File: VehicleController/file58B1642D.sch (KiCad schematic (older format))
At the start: 41 parts, among them J10 CONN_01X12, J8 CONN_01X03, J9 CONN_01X12, Q5 Q_PMOS_GSD, Q6 MC_FET, Q7 PC_FET, U16 MC_Override, U17 MCR_Shtdwn, U18 MCL_Shtdwn, U19 RI-0505S, U20 ISO1540, U21 TCMT1103, U22 TLP293-4, U23 PC_RLY, U24 MCP47FEBX2

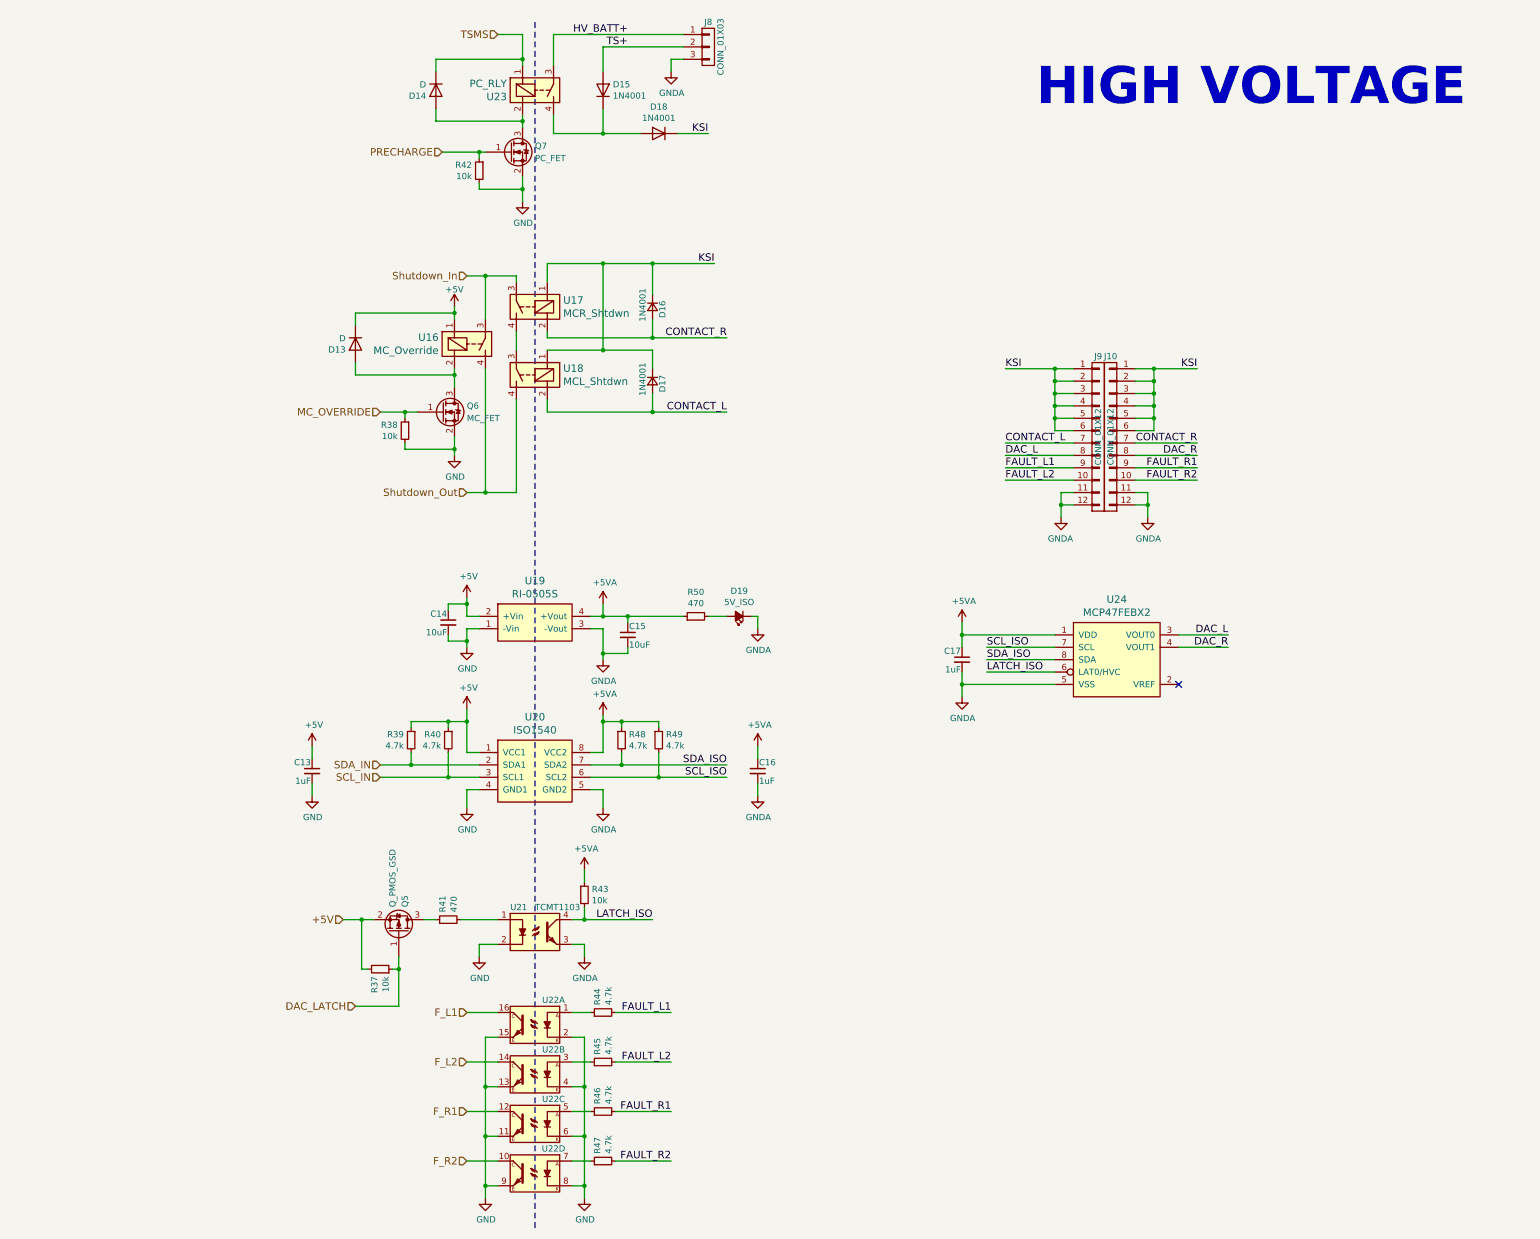
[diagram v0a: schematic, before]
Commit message: Revert "MX120, GDS->GSD FETs on VCU"
This reverts commit 5f93bf7ab8a0e63cb004bd031bee3d8b2541593f.
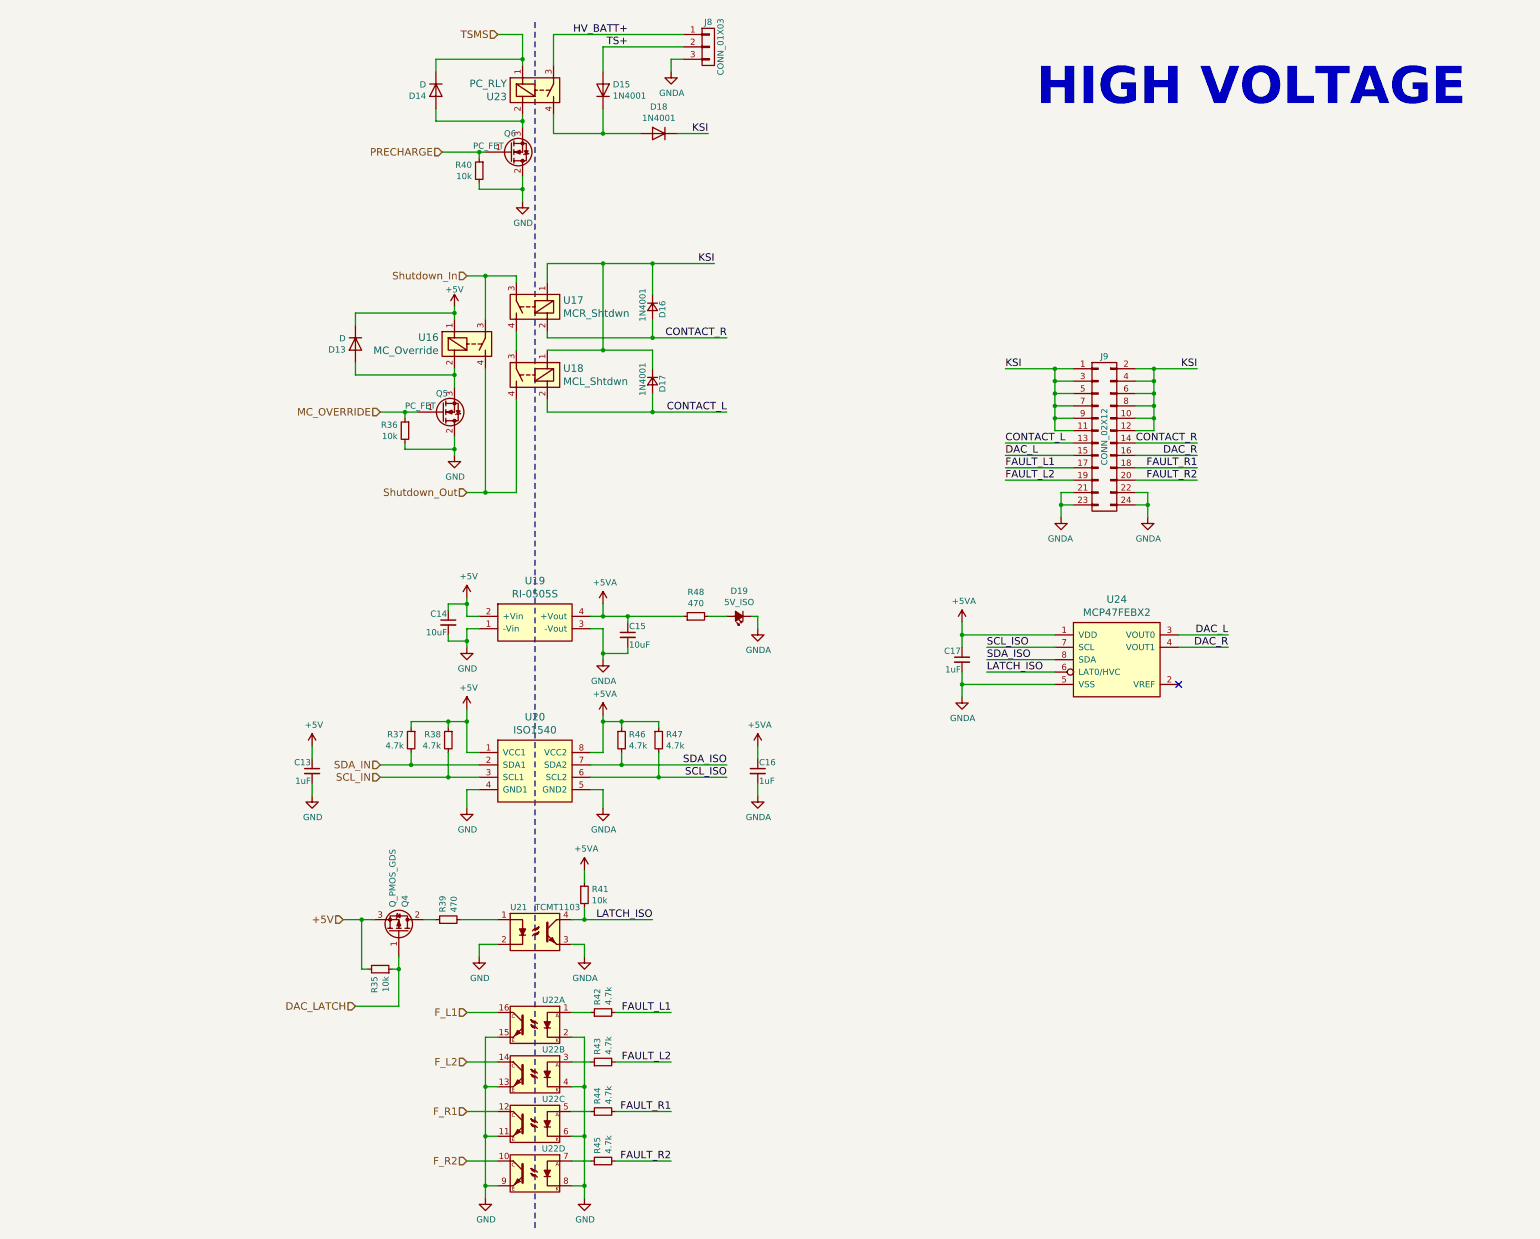
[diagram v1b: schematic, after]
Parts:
- removed J10, J9: CONN_01X12, UNCA Motorsports:MX120G-12, symbol CONN_01X12
- removed Q5: Q_PMOS_GSD, TO_SOT_Packages_SMD:SOT-23_Handsoldering, symbol Q_PMOS_GSD
- removed Q6: MC_FET, TO_SOT_Packages_SMD:SOT-23_Handsoldering, symbol Q_NMOS_GSD
- removed Q7: PC_FET, TO_SOT_Packages_SMD:SOT-23_Handsoldering, symbol Q_NMOS_GSD
- added J9: CONN_02X12, symbol CONN_02X12
- added Q4: Q_PMOS_GDS, symbol Q_PMOS_GDS
- added Q5, Q6: PC_FET, TO_SOT_Packages_SMD:SOT-23_Handsoldering, symbol Q_NMOS_GDS
- D13, D14, D15, D18: footprint Diodes_SMD:D_SMC_Handsoldering -> Diodes_SMD:SMA_Handsoldering
- D16, D17: footprint Diodes_SMD:D_SMC_Handsoldering -> (none)
- J8: footprint Pin_Headers:Pin_Header_Straight_1x03_Pitch2.54mm -> (none)
- U22: value TLP293-4 -> OPTO-TRANSISTOR-4; footprint UNCA Motorsports:SOIC16 -> (none)
- renumbered R37 to R35, R38 to R36, R39 to R37, R40 to R38, R41 to R39, R42 to R40, R43 to R41, R44 to R42, R45 to R43, R46 to R44, R47 to R45, R48 to R46, R49 to R47, R50 to R48
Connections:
- net +5V: now also Q4.3 (S)
- net CONTACT_L: now also J9.13 (P13)
- net CONTACT_R: now also J9.14 (P14)
- net DAC_L: now also J9.15 (P15)
- net DAC_LATCH: now also Q4.1 (G)
- net DAC_R: now also J9.16 (P16)
- net FAULT_L1: now also J9.17 (P17)
- net FAULT_L2: now also J9.19 (P19)
- net FAULT_R1: now also J9.18 (P18)
- net FAULT_R2: now also J9.20 (P20)
- net GND: now also Q5.2 (D), Q6.2 (D)
- net GNDA: now also J9.21 (P21), J9.22 (P22), J9.23 (P23), J9.24 (P24)
- net KSI: now also J9.1 (P1), J9.10 (P10), J9.11 (P11), J9.12 (P12), J9.2 (P2), J9.3 (P3), J9.4 (P4), J9.5 (P5), J9.6 (P6), J9.7 (P7), J9.8 (P8), J9.9 (P9)
- net MC_OVERRIDE: now also Q5.1 (G)
- net PRECHARGE: now also Q6.1 (G)
- net at R39.1: now also Q4.2 (D)
- net at D14.2 (A), U23.2: now also Q6.3 (S)
- net at D13.2 (A), U16.2: now also Q5.3 (S)

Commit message: Small changes to VCU
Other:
- moved on the sheet: C14, C15, D19, R48, U19

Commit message: Re-do MX120, GDS->GSD, Associations.
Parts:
- removed J9: CONN_02X12, symbol CONN_02X12
- removed Q4: Q_PMOS_GDS, symbol Q_PMOS_GDS
- removed Q5, Q6: PC_FET, TO_SOT_Packages_SMD:SOT-23_Handsoldering, symbol Q_NMOS_GDS
- added J10, J9: CONN_01X12, UNCA Motorsports:MX120G-12, symbol CONN_01X12
- added Q4: Q_PMOS_GSD, TO_SOT_Packages_SMD:SOT-23_Handsoldering, symbol Q_PMOS_GSD
- added Q5, Q6: Q_NMOS_GSD, TO_SOT_Packages_SMD:SOT-23_Handsoldering, symbol Q_NMOS_GSD
- D13, D14, D15, D18: footprint Diodes_SMD:SMA_Handsoldering -> Diodes_SMD:D_SMC_Handsoldering
- D16, D17: footprint (none) -> Diodes_SMD:D_SMC_Handsoldering
- J8: footprint (none) -> Pin_Headers:Pin_Header_Straight_1x03_Pitch2.54mm
- U16, U17, U18: footprint UNCAMotorsports:ALE1PB48 -> UNCA Motorsports:ALE1PB48
- U19: footprint UNCAMotorsports:RI-0505S -> UNCA Motorsports:RI-0505S
- U21: footprint UNCAMotorsports:SSOP-4 -> UNCA Motorsports:SSOP-4
- U22: footprint (none) -> UNCA Motorsports:SOIC16
- U23: footprint UNCAMotorsports:G6DN-1A -> UNCA Motorsports:G6DN-1A
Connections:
- net +5V: now also Q4.2 (S)
- net CONTACT_L: now also J9.7 (P7)
- net CONTACT_R: now also J10.7 (P7)
- net DAC_L: now also J9.8 (P8)
- net DAC_LATCH: now also Q4.1 (G)
- net DAC_R: now also J10.8 (P8)
- net FAULT_L1: now also J9.9 (P9)
- net FAULT_L2: now also J9.10 (P10)
- net FAULT_R1: now also J10.9 (P9)
- net FAULT_R2: now also J10.10 (P10)
- net GND: now also Q5.2 (S), Q6.2 (S)
- net GNDA: now also J10.11 (P11), J10.12 (P12), J9.11 (P11), J9.12 (P12)
- net KSI: now also J10.1 (P1), J10.2 (P2), J10.3 (P3), J10.4 (P4), J10.5 (P5), J10.6 (P6), J9.1 (P1), J9.2 (P2), J9.3 (P3), J9.4 (P4), J9.5 (P5), J9.6 (P6)
- net MC_OVERRIDE: now also Q5.1 (G)
- net PRECHARGE: now also Q6.1 (G)
- net at R39.1: now also Q4.3 (D)
- net at D14.2 (A), U23.2: now also Q6.3 (D)
- net at D13.2 (A), U16.2: now also Q5.3 (D)

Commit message: Library Fixes
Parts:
- D13, D14, D15, D16, D17, D18: footprint Diodes_SMD:D_SMC_Handsoldering -> Diodes_SMD:SMC_Handsoldering
- J10, J9: footprint UNCA Motorsports:MX120G-12 -> UNCAMotorsports:MX120G-12
- J8: footprint Pin_Headers:Pin_Header_Straight_1x03_Pitch2.54mm -> Pin_Headers:Pin_Header_Straight_1x03
- U16, U17, U18: footprint UNCA Motorsports:ALE1PB48 -> UNCAMotorsports:ALE1PB48
- U19: footprint UNCA Motorsports:RI-0505S -> UNCAMotorsports:RI-0505S
- U21: footprint UNCA Motorsports:SSOP-4 -> UNCAMotorsports:SSOP-4
- U22: footprint UNCA Motorsports:SOIC16 -> UNCAMotorsports:SOIC16
- U23: footprint UNCA Motorsports:G6DN-1A -> UNCAMotorsports:G6DN-1A
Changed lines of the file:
@@
 F 0 "U19" H 7350 5587 60  0000 C CNN
 F 1 "RI-0505S" H 7350 5481 60  0000 C CNN
-F 2 "UNCA Motorsports:RI-0505S" H 7350 5250 60  0001 C CNN
+F 2 "UNCAMotorsports:RI-0505S" H 7350 5250 60  0001 C CNN
 F 3 "" H 7350 5250 60  0001 C CNN
 	1    7350 5250
@@
 F 0 "U17" V 7197 3228 60  0000 L CNN
 F 1 "MCR_Shtdwn" V 7303 3228 60  0000 L CNN
-F 2 "UNCA Motorsports:ALE1PB48" H 7250 2950 60  0001 C CNN
+F 2 "UNCAMotorsports:ALE1PB48" H 7250 2950 60  0001 C CNN
 F 3 "" H 7250 2950 60  0001 C CNN
 	1    7250 2950
@@
 F 0 "U18" V 7197 3778 60  0000 L CNN
 F 1 "MCL_Shtdwn" V 7303 3778 60  0000 L CNN
-F 2 "UNCA Motorsports:ALE1PB48" H 7250 3500 60  0001 C CNN
+F 2 "UNCAMotorsports:ALE1PB48" H 7250 3500 60  0001 C CNN
 F 3 "" H 7250 3500 60  0001 C CNN
 	1    7250 3500
@@
 F 0 "U23" V 7403 1477 60  0000 L CNN
 F 1 "PC_RLY" V 7297 1477 60  0000 L CNN
-F 2 "UNCA Motorsports:G6DN-1A" H 7350 1200 60  0001 C CNN
+F 2 "UNCAMotorsports:G6DN-1A" H 7350 1200 60  0001 C CNN
 F 3 "" H 7350 1200 60  0001 C CNN
 	1    7350 1200
@@
 F 0 "D18" H 8300 1766 50  0000 C CNN
 F 1 "1N4001" H 8300 1675 50  0000 C CNN
-F 2 "Diodes_SMD:D_SMC_Handsoldering" H -2300 450 50  0001 C CNN
+F 2 "Diodes_SMD:SMC_Handsoldering" H -2300 450 50  0001 C CNN
 F 3 "" H -2300 450 50  0001 C CNN
 	1    8300 1550
@@
 F 0 "D15" V 7896 1279 50  0000 L CNN
 F 1 "1N4001" V 7805 1279 50  0000 L CNN
-F 2 "Diodes_SMD:D_SMC_Handsoldering" H -2750 100 50  0001 C CNN
+F 2 "Diodes_SMD:SMC_Handsoldering" H -2750 100 50  0001 C CNN
 F 3 "" H -2750 100 50  0001 C CNN
 	1    7850 1200
@@
 F 0 "D14" V 6546 1279 50  0000 L CNN
 F 1 "D" V 6455 1279 50  0000 L CNN
-F 2 "Diodes_SMD:D_SMC_Handsoldering" H -4100 100 50  0001 C CNN
+F 2 "Diodes_SMD:SMC_Handsoldering" H -4100 100 50  0001 C CNN
 F 3 "" H -4100 100 50  0001 C CNN
 	1    6500 1200
@@
 F 0 "U21" H 7100 8200 50  0000 L CNN
 F 1 "TCMT1103" H 7300 8200 50  0000 L CNN
-F 2 "UNCA Motorsports:SSOP-4" H 7100 7800 50  0001 L CIN
+F 2 "UNCAMotorsports:SSOP-4" H 7100 7800 50  0001 L CIN
 F 3 "" H 7300 8000 50  0001 L CNN
 	1    7300 8000
@@
 F 0 "U22" H 7150 8950 50  0000 C CNN
 F 1 "OPTO-TRANSISTOR-4" H 7300 8984 50  0001 C CNN
-F 2 "UNCA Motorsports:SOIC16" H -2250 4300 50  0001 L CIN
+F 2 "UNCAMotorsports:SOIC16" H -2250 4300 50  0001 L CIN
 F 3 "" H -2050 4500 50  0001 L CNN
 	1    7300 8750
@@
 F 0 "U22" H 7150 9350 50  0000 C CNN
 F 1 "OPTO-TRANSISTOR-4" H 7300 9384 50  0001 C CNN
-F 2 "UNCA Motorsports:SOIC16" H -2250 4700 50  0001 L CIN
+F 2 "UNCAMotorsports:SOIC16" H -2250 4700 50  0001 L CIN
 F 3 "" H -2050 4900 50  0001 L CNN
 	2    7300 9150
@@
 F 0 "U22" H 7150 9750 50  0000 C CNN
 F 1 "OPTO-TRANSISTOR-4" H 7300 9784 50  0001 C CNN
-F 2 "UNCA Motorsports:SOIC16" H -2250 5100 50  0001 L CIN
+F 2 "UNCAMotorsports:SOIC16" H -2250 5100 50  0001 L CIN
 F 3 "" H -2050 5300 50  0001 L CNN
 	3    7300 9550
@@
 F 0 "U22" H 7150 10150 50  0000 C CNN
 F 1 "OPTO-TRANSISTOR-4" H 7300 10184 50  0001 C CNN
-F 2 "UNCA Motorsports:SOIC16" H -2250 5500 50  0001 L CIN
+F 2 "UNCAMotorsports:SOIC16" H -2250 5500 50  0001 L CIN
 F 3 "" H -2050 5700 50  0001 L CNN
 	4    7300 9950
@@
 F 0 "J8" H 8700 1050 50  0000 C CNN
 F 1 "CONN_01X03" V 8800 850 50  0000 C CNN
-F 2 "Pin_Headers:Pin_Header_Straight_1x03_Pitch2.54mm" H 8700 850 50  0001 C CNN
+F 2 "Pin_Headers:Pin_Header_Straight_1x03" H 8700 850 50  0001 C CNN
 F 3 "" H 8700 850 50  0001 C CNN
 	1    8700 850
@@
 F 0 "D17" H 8200 3630 50  0000 L CNN
 F 1 "1N4001" H 8100 3470 50  0000 L CNN
-F 2 "Diodes_SMD:D_SMC_Handsoldering" V 8250 3550 50  0001 C CNN
+F 2 "Diodes_SMD:SMC_Handsoldering" V 8250 3550 50  0001 C CNN
 F 3 "" V 8250 3550 50  0001 C CNN
 	1    8250 3550
@@
 F 0 "D16" H 8200 3030 50  0000 L CNN
 F 1 "1N4001" H 8100 2870 50  0000 L CNN
-F 2 "Diodes_SMD:D_SMC_Handsoldering" V 8250 2950 50  0001 C CNN
+F 2 "Diodes_SMD:SMC_Handsoldering" V 8250 2950 50  0001 C CNN
 F 3 "" V 8250 2950 50  0001 C CNN
 	1    8250 2950
@@
 F 0 "U16" V 6747 3528 60  0000 L CNN
 F 1 "MC_Override" V 6853 3528 60  0000 L CNN
-F 2 "UNCA Motorsports:ALE1PB48" H 6800 3250 60  0001 C CNN
+F 2 "UNCAMotorsports:ALE1PB48" H 6800 3250 60  0001 C CNN
 F 3 "" H 6800 3250 60  0001 C CNN
 	1    6800 3250
@@
 F 0 "D13" V 5896 3329 50  0000 L CNN
 F 1 "D" V 5805 3329 50  0000 L CNN
-F 2 "Diodes_SMD:D_SMC_Handsoldering" H -4750 2150 50  0001 C CNN
+F 2 "Diodes_SMD:SMC_Handsoldering" H -4750 2150 50  0001 C CNN
 F 3 "" H -4750 2150 50  0001 C CNN
 	1    5850 3250
@@
 F 0 "J9" H 11850 4650 50  0000 C CNN
 F 1 "CONN_01X12" V 11950 4000 50  0000 C CNN
-F 2 "UNCA Motorsports:MX120G-12" H 11850 4000 50  0001 C CNN
+F 2 "UNCAMotorsports:MX120G-12" H 11850 4000 50  0001 C CNN
 F 3 "" H 11850 4000 50  0001 C CNN
 	1    11850 4000
@@
 F 0 "J10" H 11950 4650 50  0000 C CNN
 F 1 "CONN_01X12" V 12050 4000 50  0000 C CNN
-F 2 "UNCA Motorsports:MX120G-12" H 11950 4000 50  0001 C CNN
+F 2 "UNCAMotorsports:MX120G-12" H 11950 4000 50  0001 C CNN
 F 3 "" H 11950 4000 50  0001 C CNN
 	1    11950 4000
